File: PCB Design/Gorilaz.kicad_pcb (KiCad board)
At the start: 2 copper layers, 100 x 86 mm, 51 parts, among them J1 Conn_01x13, J2 Conn_01x13, J3 Conn_01x13, J4 Conn_01x13, J5 Conn_01x13, J6 Conn_01x13, J7 Battery, J8 HRO_TYPE-C-31-M-14, M1 MountingHole_6.4mm_M6, M3 MountingHole_4.3mm_M4, M4 MountingHole_4.3mm_M4, SW4 RST, U1 SRV05-4, U10 MAX17048, U3 BQ24075, U4 DW01A, U5 FS8205, U8 nRF52840_moko_mk08

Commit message: update pre-prod
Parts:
- D1, D2, D3: footprint LED_SMD:LED_1206_3216Metric -> LED_SMD:LED_1206_3216Metric_ReverseMount_Hole1.8x2.4mm; moved to F.Cu
- J7: footprint Connector_JST:JST_GH_BM02B-GHS-TBT_1x02-1MP_P1.25mm_Vertical -> Connector_JST:JST_PH_B2B-PH-K_1x02_P2.00mm_Vertical
- moved J7 6.07 mm to (133.9, 115.8), turned to 0 degrees
- turned D1 to 0 degrees
- turned D2 to 0 degrees
- turned D3 to 0 degrees
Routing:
- net +5V: track 63.6 -> 58.6 mm
- net Net-(D3-A): track 3.74 -> 0.00 mm, vias 1 -> 0
- net Net-(D2-A): track 3.74 -> 0.00 mm, vias 1 -> 0
- net Net-(D1-A): track 3.74 -> 0.00 mm, vias 1 -> 0
- net Net-(J7-Pin_2): track 27.8 -> 24.7 mm
- net LED_POWER_ON: track 56.1 -> 58.4 mm
- net row14: track 156.7 -> 154.8 mm
- net row12: track 129.1 -> 127.5 mm
- net USB-D-: track 43.5 -> 42.0 mm
- net +BATT: track 58.0 -> 56.5 mm, vias 1 -> 0
- net col5: track 261.1 -> 259.8 mm
- net GND: track 46.6 -> 47.7 mm, vias 35 -> 41
- net LED_BLE: track 47.0 -> 48.1 mm
- net col0: track 168.3 -> 169.3 mm
- net col4: track 166.0 -> 165.2 mm
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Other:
- board text added: "Batt Warn"
- board text added: "Chassis switch ->"
- board text removed: "Chassis switch"

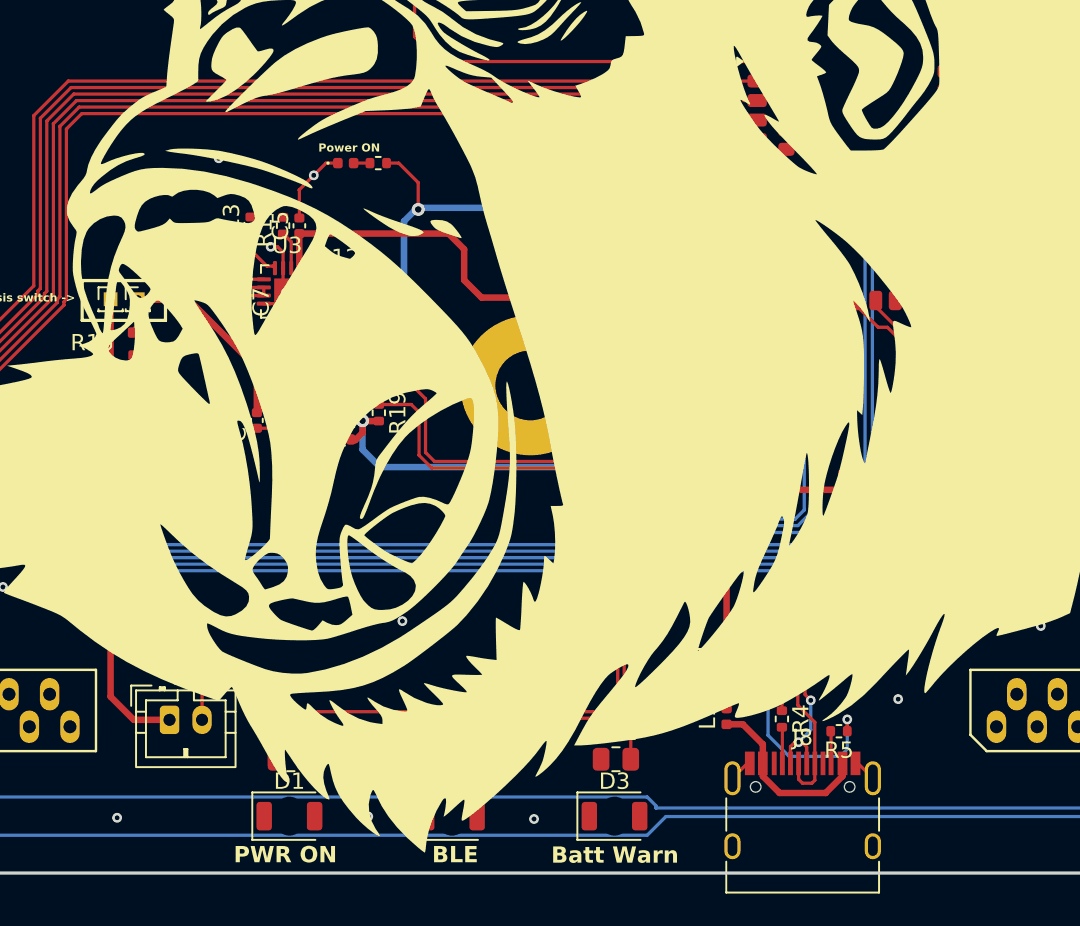
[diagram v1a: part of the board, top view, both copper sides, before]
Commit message: ESD update
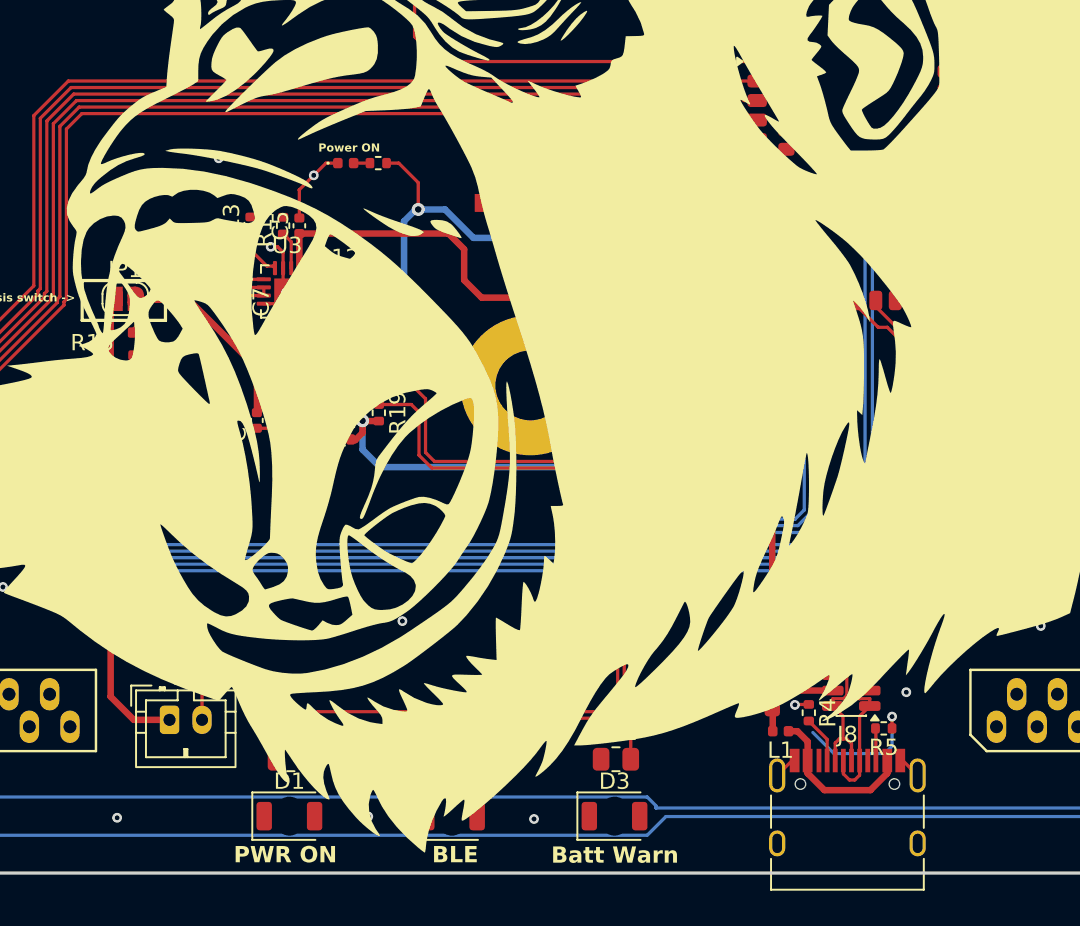
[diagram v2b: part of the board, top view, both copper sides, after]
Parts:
- removed REF** (x2): PinHeader_1x01_P1.00mm_Vertical, Connector_PinHeader_1.00mm:PinHeader_1x01_P1.00mm_Vertical
- added J9: TC2030_SWD, Mastarlib:CON_TC2030_outlined, F.Cu at (180.2, 100.6)
- added JP1: power on, Jumper:SolderJumper-2_P1.3mm_Open_RoundedPad1.0x1.5mm, F.Cu at (131.2, 89.9)
- moved U1 12.4 mm to (175.9, 114.0)
- moved F1 3.76 mm to (171.0, 114.3)
- moved L1 3.45 mm to (171.5, 116.5), turned to 180 degrees
- moved J8 2.76 mm to (175.7, 122.3)
- moved R5 2.76 mm to (177.9, 116.3)
- moved SW4 2.23 mm to (156.7, 82.1)
- moved R4 1.70 mm to (173.3, 115.3)
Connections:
- U1 pad 1: USB-D- -> unconnected-(U1-IO1-Pad1)
- U1 pad 6: USB-D+ -> unconnected-(U1-IO4-Pad6)
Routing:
- net Net-(J7-Pin_1): track 0.00 -> 28.7 mm
- net +BATT: track 56.5 -> 27.8 mm
- net USB-D+: track 44.0 -> 41.0 mm
- net GND: track 47.7 -> 44.7 mm, vias 41 -> 43
- net RST: track 29.4 -> 31.3 mm
- net +VSW: track 48.4 -> 49.8 mm
- net VBUS: track 11.2 -> 9.94 mm
- net Net-(F1-Pad1): track 2.45 -> 1.36 mm
- net Net-(J8-CC1): track 2.23 -> 2.90 mm
- net USB-D-: track 42.0 -> 41.4 mm, vias 4 -> 2

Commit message: lots of improvement
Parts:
- removed C7: 4u7, Capacitor_SMD:C_0402_1005Metric
- removed J9: TC2030_SWD, Mastarlib:CON_TC2030_outlined
- removed JP1: power on, Jumper:SolderJumper-2_P1.3mm_Open_RoundedPad1.0x1.5mm
- removed the R4 at (173.3, 115.3)
- removed the R5 at (177.9, 116.3)
- added C3: 4u7, Capacitor_SMD:C_0402_1005Metric, F.Cu at (137.9, 76.8)
- added CN1: 950-D-SMD-DS/02, easyeda:CONN-SMD_2P-P5.00_950-D-SMD-DS-02, F.Cu at (132.2, 59.4)
- added R1: 5k1, Resistor_SMD:R_0402_1005Metric, F.Cu at (171.4, 73.5)
- added R2: 5k1, Resistor_SMD:R_0402_1005Metric, F.Cu at (175.6, 73.5)
- added USB1: USB-310M-B-SU, easyeda:USB-C-SMD_USB-310M-B-SU, F.Cu at (173.3, 78.0)
- J8: value HRO_TYPE-C-31-M-14 -> Conn_01x05_MountingPin; footprint Connector_USB:USB_C_Receptacle_HRO_TYPE-C-31-M-12 -> Connector_PinHeader_2.54mm:PinHeader_1x05_P2.54mm_Vertical
- moved J8 82.7 mm to (136.3, 49.6), turned to 90 degrees
- moved U1 42.9 mm to (173.2, 71.2)
- moved L1 42.7 mm to (168.2, 73.9)
- moved F1 42.1 mm to (168.5, 72.3), turned to 0 degrees
- moved U8 28.9 mm to (173.6, 51.0)
- moved SW1 26.2 mm to (143.1, 59.7)
- moved R6 13.4 mm to (143.9, 75.2)
- moved C2 13.3 mm to (141.4, 72.1)
- moved C5 13.3 mm to (138.8, 84.1)
- moved D1 13.3 mm to (144.9, 79.4)
- moved D2 13.3 mm to (144.2, 68.2)
- moved R10 13.3 mm to (146.2, 68.2)
- moved R11 13.3 mm to (144.0, 85.2)
- moved R13 13.3 mm to (146.3, 83.6)
- moved R3 13.3 mm to (131.6, 78.7)
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- renumbered C8 to C1, C5 to C2, C6 to C4, C17 to C5, LED2 to D1, LED1 to D2, D1 to D3, D2 to D4, D3 to D5, R1 to R10, R2 to R11, R18 to R12, R19 to R13, R20 to R14, R21 to R15, R22 to R16, R15 to R3, R17 to R4, R11 to R5, R12 to R6, R13 to R7, R9 to R8, R10 to R9, SW4 to SW1, U5 to U2, U4 to U3, U3 to U4, U10 to U5
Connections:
- U8 pad 22: col2 -> row0
- U8 pad 23: col1 -> row1
- U8 pad 24: row0 -> row2
- U8 pad 25: row1 -> row3
- U8 pad 26: row2 -> row4
- U8 pad 28: row3 -> row5
- U8 pad 29: row4 -> col1
- U8 pad 30: row5 -> col2
- U8 pad 33: col0 -> row12
- U8 pad 34: row12 -> col0
- U8 pad 54: unconnected-(U8-P1.05-LF-Pad54) -> ALERT
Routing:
- net ALERT: track 1.80 -> 65.8 mm, vias 0 -> 4
- net SWDIO: track 0.00 -> 50.3 mm, vias 0 -> 3
- net SWDCLK: track 0.00 -> 42.4 mm, vias 0 -> 3
- net row12: track 127.5 -> 87.8 mm
- net LED_BATT_WARN: track 38.4 -> 77.7 mm, vias 2 -> 1
- net col6: track 123.1 -> 159.8 mm
- net LED_BLE: track 48.1 -> 84.8 mm, vias 2 -> 1
- net col4: track 165.2 -> 201.6 mm
- net LED_POWER_ON: track 58.4 -> 94.0 mm, vias 2 -> 1
- net col3: track 162.2 -> 197.1 mm
- net +3.3V: track 47.0 -> 81.2 mm, vias 3 -> 4
- net row14: track 154.8 -> 124.0 mm, vias 8 -> 7
- net Net-(J7-Pin_1): track 28.7 -> 59.4 mm
- net row0: track 21.6 -> 52.0 mm
- net row3: track 41.4 -> 71.2 mm
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
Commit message: clean up
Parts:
- J8: footprint Connector_PinHeader_2.54mm:PinHeader_1x05_P2.54mm_Vertical -> Connector_PinHeader_2.54mm:PinHeader_1x05_P2.54mm_Vertical_SMD_Pin1Left
- moved G*** 22.7 mm to (179.2, 85.5)
- moved J8 5.06 mm to (141.2, 48.2)
- turned CN1 to 180 degrees
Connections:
- R14 pad 2: LED_POWER_ON -> LED_BATT_WARN
- R16 pad 2: LED_BATT_WARN -> LED_POWER_ON
- U8 pad 13: LED_POWER_ON -> LED_BATT_WARN
- U8 pad 15: LED_BATT_WARN -> LED_POWER_ON
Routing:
- net LED_POWER_ON: track 94.0 -> 60.5 mm, vias 1 -> 0
- net LED_BLE: track 84.8 -> 69.5 mm, vias 1 -> 0
- net row12: track 87.8 -> 90.7 mm
- net SWDIO: track 50.3 -> 53.1 mm, vias 3 -> 4
- net col5: track 231.9 -> 234.4 mm
- net row14: track 124.0 -> 126.4 mm
- net SWDCLK: track 42.4 -> 44.5 mm, vias 3 -> 4
- net row13: track 128.3 -> 130.1 mm
- net LED_BATT_WARN: track 77.7 -> 78.8 mm, vias 1 -> 0
- net +3.3V: track 81.2 -> 82.1 mm, vias 4 -> 5
- net RST: track 51.9 -> 52.0 mm, vias 2 -> 3
- net GND: vias 51 -> 55
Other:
- board text added: "3.3V"
- board text added: "Battery"
- board text added: "Case Switch"
- board text added: "GND"
- board text added: "Gorillaz Board V0.1 Feb 2026 https://github.com/nol00p/Gorillaz"
- board text added: "RST"
- board text added: "Reset"
- board text added: "SWDCLK"
- board text added: "SWDIO"
- board text removed: "Chassis switch ->"
- board text removed: "Gorillaz Board V0 Feb 2026 https://github.com/nol00p/Gorillaz"
- board text removed: "Power ON"

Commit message: LED update
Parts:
- D1: value Charing -> LED_PWON; footprint LED_SMD:LED_0402_1005Metric -> LED_SMD:LED_1206_3216Metric_ReverseMount_Hole1.8x2.4mm
- D3: value LED_CAPS -> LED_BATT_WARN
- D4: value LED_NUM -> LED_CHARGING
- D5: value LED_SCR -> LED_BLE
- moved D1 49.9 mm to (171.3, 121.7), turned to 0 degrees
- moved R9 41.1 mm to (149.7, 119.0)
- moved R16 8.57 mm to (170.0, 118.5), turned to 90 degrees
- moved R15 8.56 mm to (160.0, 118.3), turned to 90 degrees
- moved R14 1.23 mm to (142.6, 118.4), turned to 90 degrees
- turned D4 to 180 degrees
- turned D5 to 180 degrees
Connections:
- D1 pad 1: Net-(D1-K) -> Net-(D1-A)
- D1 pad 2: +VSW -> GND
- D4 pad 1: GND -> +VSW
- D4 pad 2: Net-(D4-A) -> Net-(D4-K)
- R15 pad 1: Net-(D4-A) -> Net-(D5-A)
- R16 pad 1: Net-(D5-A) -> Net-(D1-A)
- R9 pad 1: Net-(D1-K) -> Net-(D4-K)
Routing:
- net +VSW: track 60.4 -> 111.4 mm, vias 3 -> 5
- net Net-(U4-~{CHG}): track 2.33 -> 50.5 mm, vias 0 -> 4
- net LED_BLE: track 69.5 -> 61.2 mm
- net LED_POWER_ON: track 60.5 -> 66.8 mm
- net col5: track 234.4 -> 239.1 mm
- net Net-(D5-A): track 0.00 -> 2.55 mm
- net Net-(D3-A): track 0.00 -> 2.49 mm
- net Net-(D1-A): track 0.00 -> 2.42 mm
- net Net-(D4-K): track 0.00 -> 2.22 mm
- net col6: track 159.8 -> 161.8 mm
- net Net-(D1-K): track 1.25 -> 0.00 mm
- net LED_BATT_WARN: track 78.8 -> 78.0 mm
- net GND: vias 55 -> 58
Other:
- board text added: "power on debug"

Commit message: LED update
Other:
- board text added: "Batt Charg"
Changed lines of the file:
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@@
+			)
+		)
+		(model "/home/skullbocks/Documents/Kicad/3D Lib/D_1206_3216Metric.wrl"
+			(offset
+				(xyz 0 0 0)
+			)
+			(scale
+				(xyz 1 1 1)
+			)
+			(rotate
+				(xyz 0 0 0)
 			)
 		)
@@
 	)
 	(gr_text "PWR ON"
-		(at 161.35 124.325 0)
+		(at 171.225 124.25 0)
 		(layer "F.SilkS")
 		(effects
@@
 	)
 	(gr_text "BLE"
-		(at 151.525 124.075 0)
-		(layer "F.SilkS")
-		(effects
+		(at 161.4 124 0)
+		(layer "F.SilkS")
+		(effects
+			(font
+				(size 1 1)
+				(thickness 0.2)
+				(bold yes)
+			)
+		)
+	)
+	(gr_text "Batt Charg"
+		(at 151.975 124.125 0)
+		(layer "F.SilkS")
+		(effects
